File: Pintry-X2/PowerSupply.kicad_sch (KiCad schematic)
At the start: 36 parts, among them J11 54-00131, Q5 SIA483DJ, Q6 BC857BW, Q7 SIA483DJ, U13 AP62600

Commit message: Cleaned up schematic
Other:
- note added: "5V Power Supply"
- note added: "Power Supply Input"
- moved on the sheet: C57, C58, C59, C60, C61, C62, C63, C64, L2, R22, R23, R24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

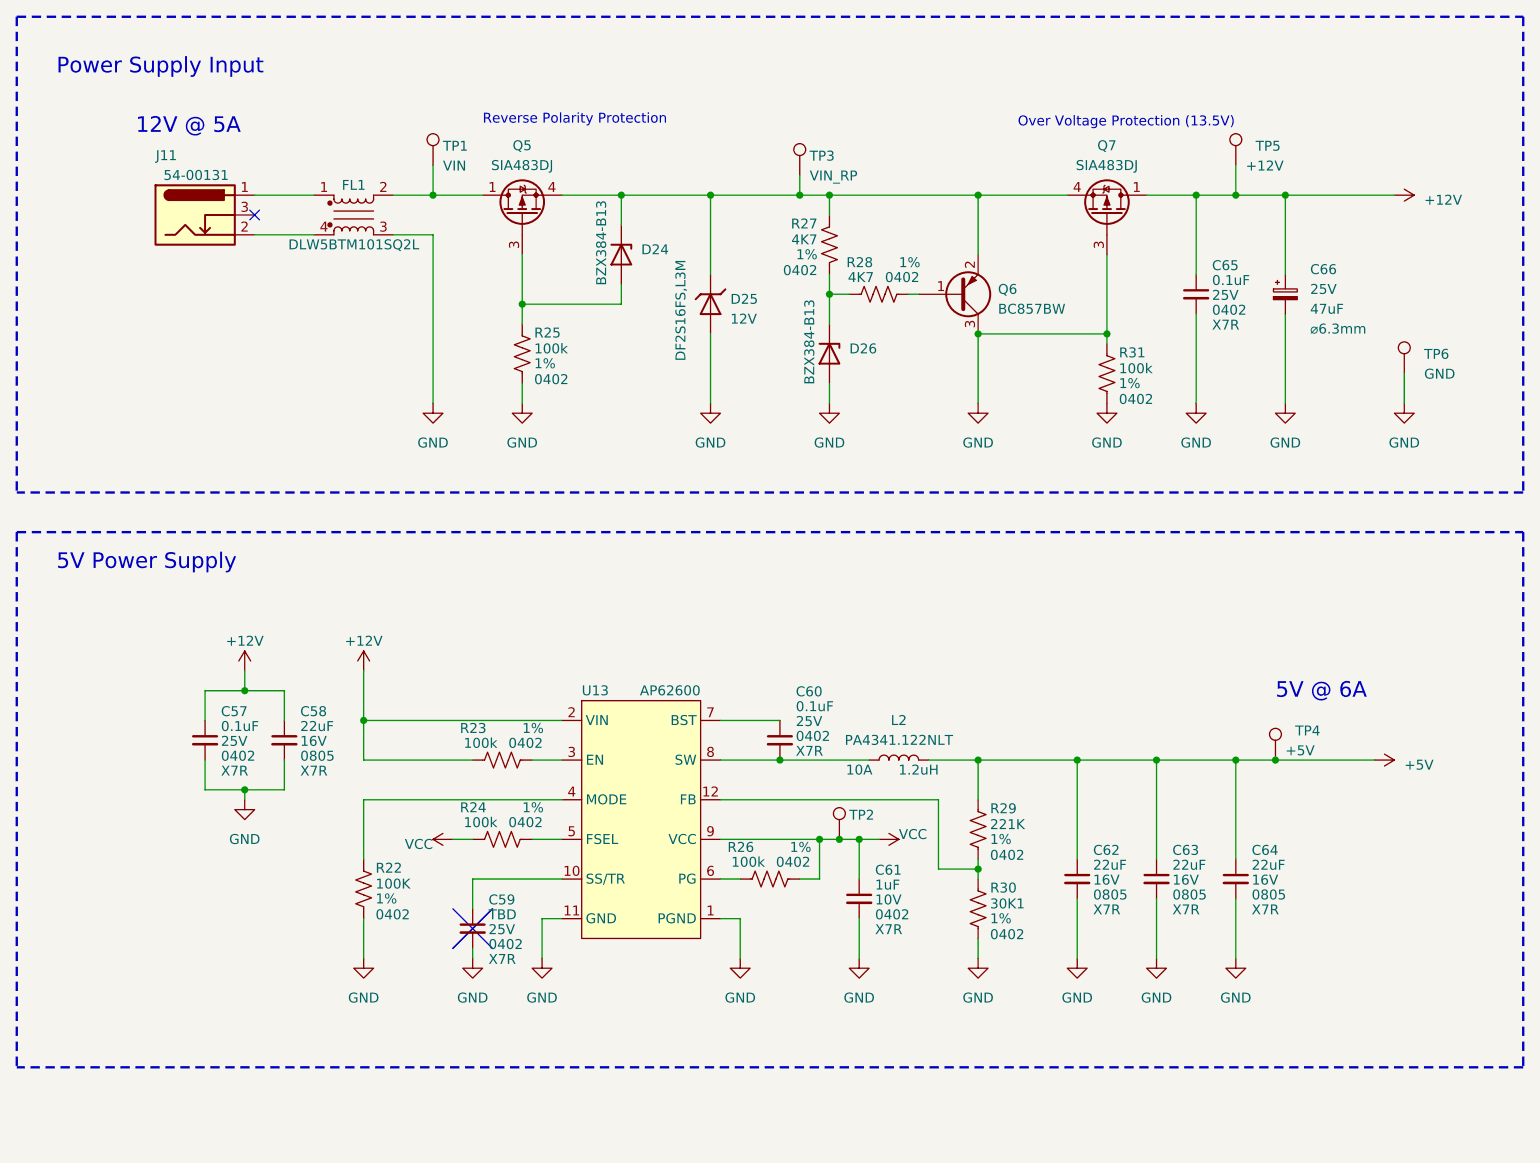
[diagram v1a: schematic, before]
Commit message: Finished Shematic. Starting PCB
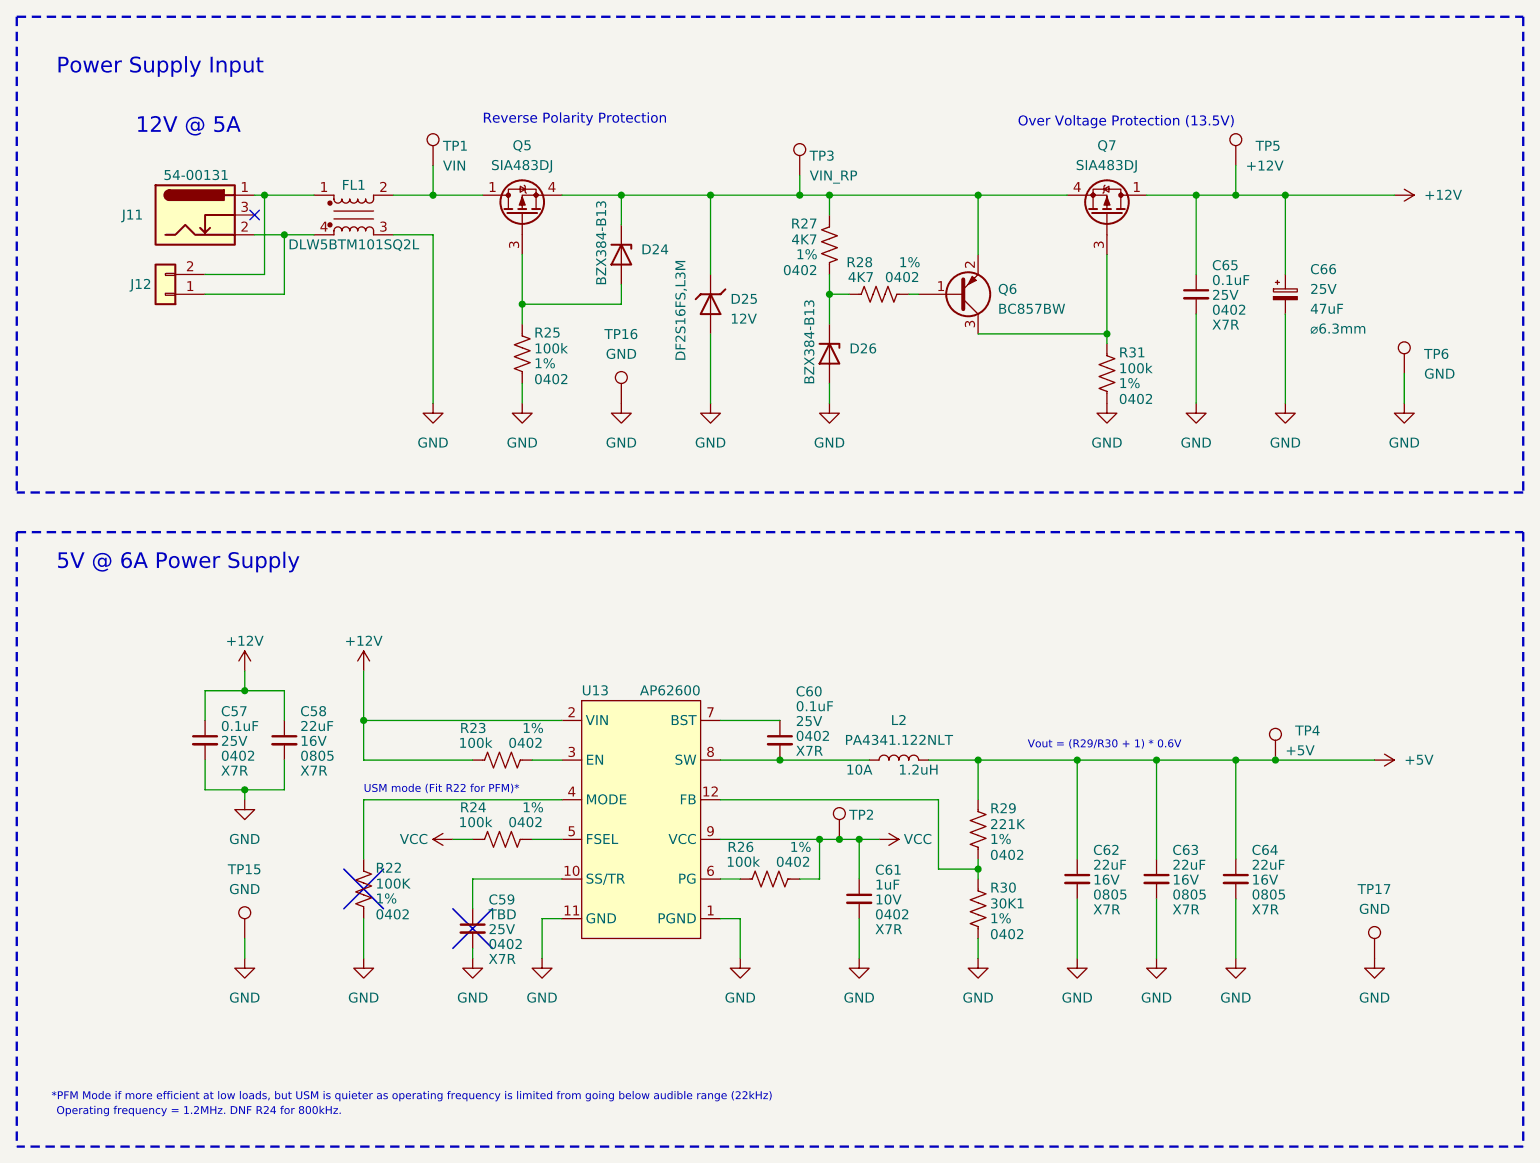
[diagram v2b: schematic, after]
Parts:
- added J12: Alternate Power Connector, Connector_Wire:SolderWire-1sqmm_1x02_P5.4mm_D1.4mm_OD2.7mm, symbol Connector_Generic:Conn_01x02
- added TP15, TP16, TP17: GND, TestPoint:TestPoint_Pad_D1.0mm, symbol Connector:TestPoint
- C59: fit_field (none) -> dnf; now in the parts list
- R22: fit_field (none) -> dnf
- TP1, TP2, TP3, TP4, TP5, TP6: footprint TestPoint:TestPoint_Pad_D2.5mm -> TestPoint:TestPoint_Pad_D1.0mm
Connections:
- net GND: now also TP15.1, TP16.1, TP17.1; no longer Q6.3 (C), Q7.3 (G), R31.1
- net at FL1.1, J11.1 (A): now also J12.2 (Pin_2)
- net at FL1.4, J11.2 (B): now also J12.1 (Pin_1)
- new net: Q6.3 (C), Q7.3 (G), R31.1
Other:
- note added: "*PFM Mode if more efficient at low loads, but USM is quieter as operating frequency is limited from going below audible range (22kHz)"
- note added: "5V @ 6A Power Supply"
- note added: "Operating frequency = 1.2MHz. DNF R24 for 800kHz."
- note added: "USM mode (Fit R22 for PFM)*"
- note added: "Vout = (R29/R30 + 1) * 0.6V"
- note removed: "5V @ 6A"
- note removed: "5V Power Supply"

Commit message: PCB Routing Complete - needs review
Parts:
- Q5, Q7: footprint Package_TO_SOT_SMD:Vishay_PowerPAK_SC70-6L_Single -> PintryParts-Footprints:Vishay_PowerPAK_SC70-6L_Single
- TP1, TP15, TP16, TP17, TP2, TP3, TP4, TP5, TP6: footprint TestPoint:TestPoint_Pad_D1.0mm -> PintryParts-Footprints:TestPoint_Pad_D1.0mm

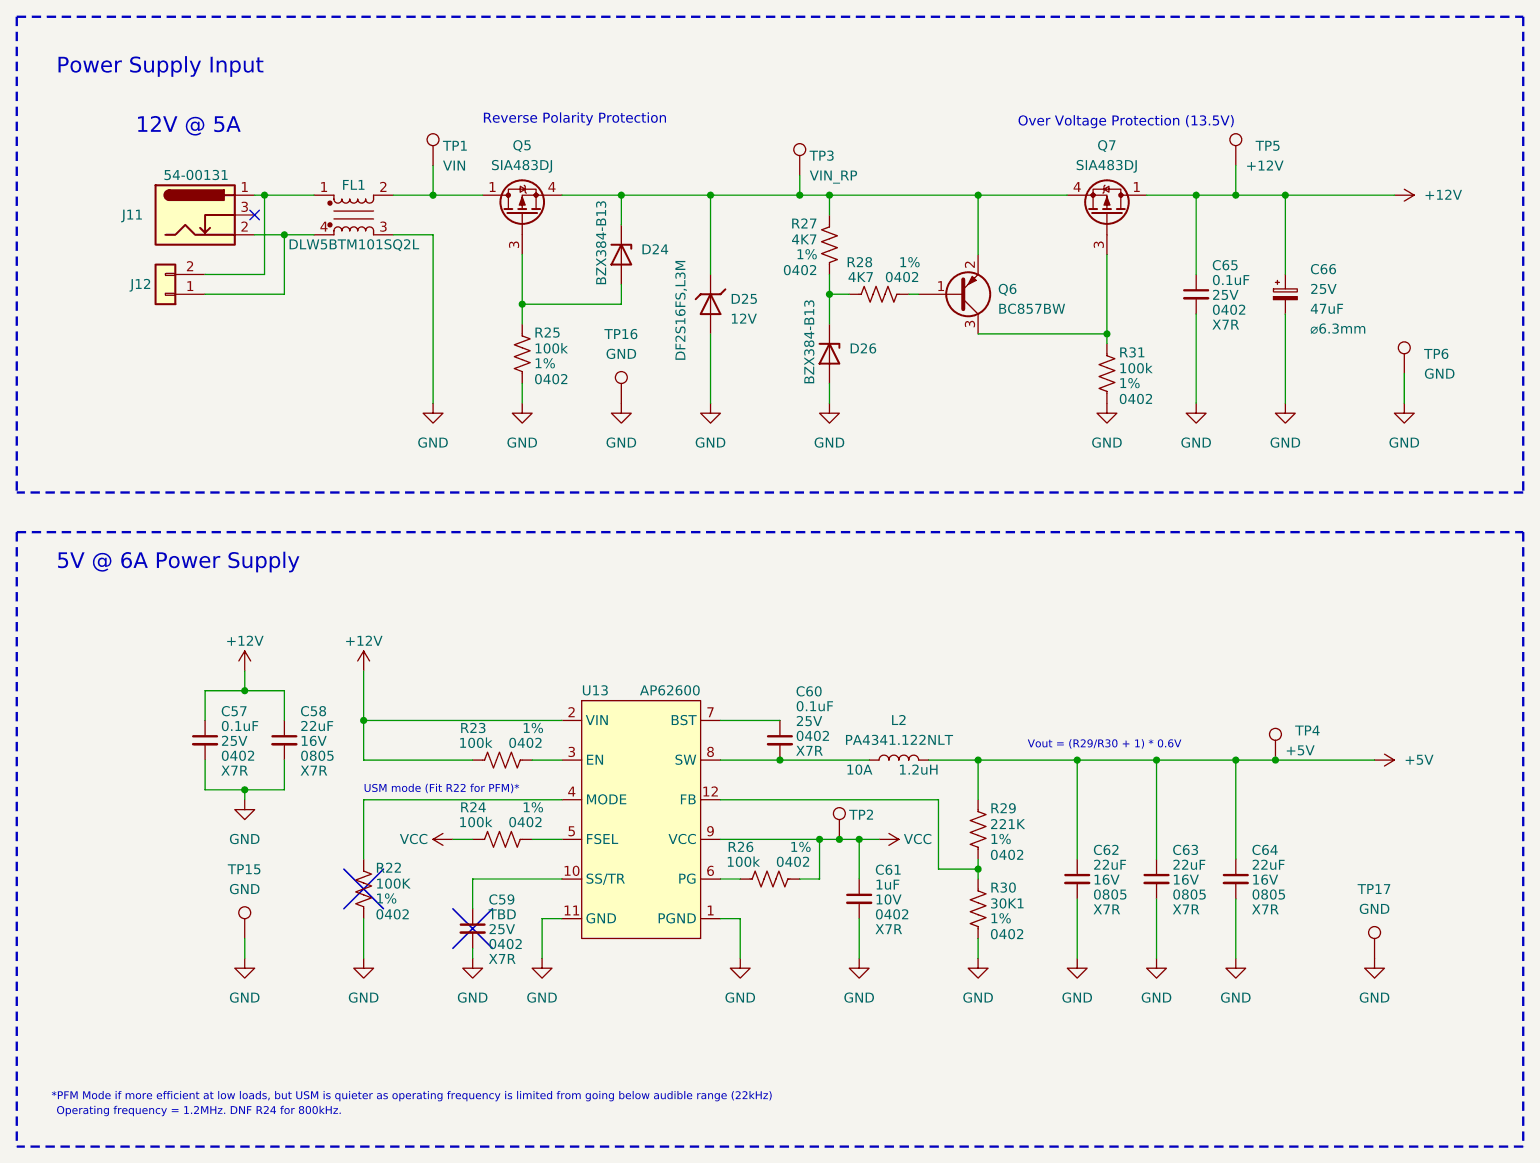
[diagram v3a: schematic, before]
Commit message: Final touches and generate Gerbers to be sent to fab
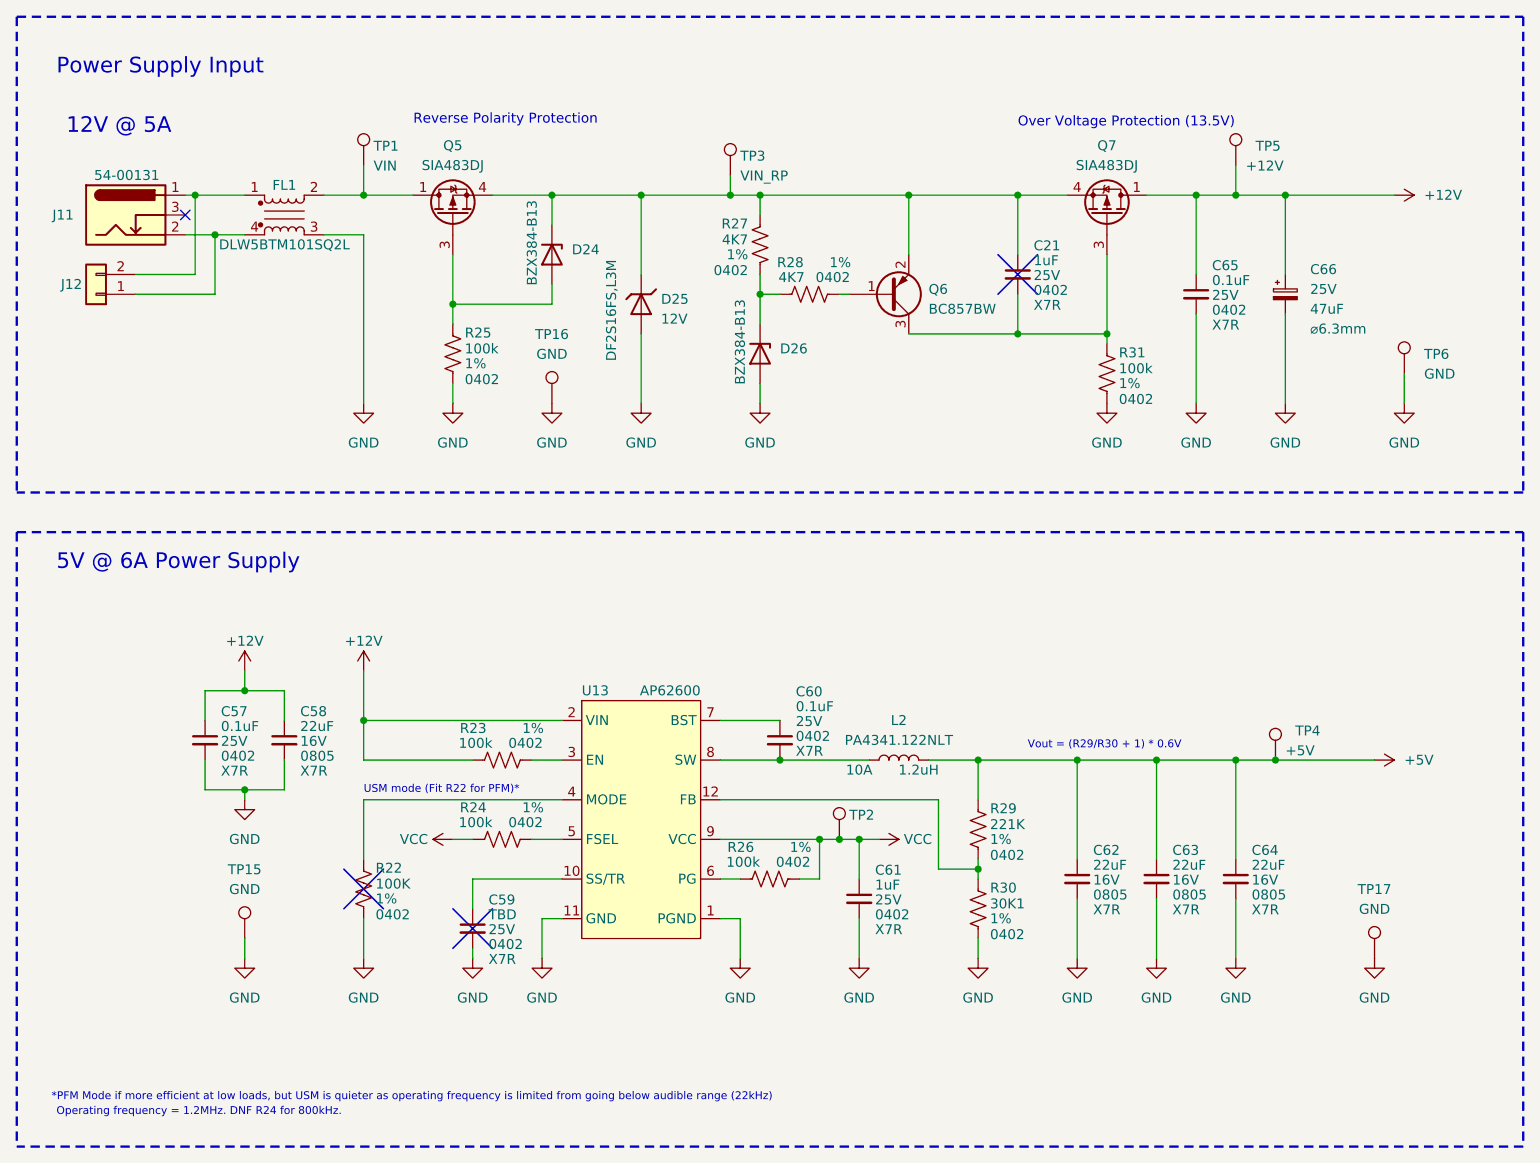
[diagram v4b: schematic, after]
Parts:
- added C21: 1uF, PintryParts-Footprints:C_0402_1005Metric, symbol Device:C_Small
- C61: Voltage Rating 10V -> 25V
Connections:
- net at D24.1 (K), D25.1 (K), Q5.4 (S)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: now also C21.1
- net at Q6.3 (C), Q7.3 (G), R31.1: now also C21.2
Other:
- moved on the sheet: D24, D25, D26, FL1, J11, J12, Q5, Q6, R25, R27, R28, TP1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
